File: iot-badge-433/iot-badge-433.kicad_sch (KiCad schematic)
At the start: 62 parts, among them J1 USB_C_Receptacle_USB2.0, J2 Wire ANT, Q1 BC847, Q2 BC847, Q3 BC847, SW1 SW_Push, SW2 SW_Push, SW3 SW_Push, SW4 SW_Push, SW5 SW_Push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

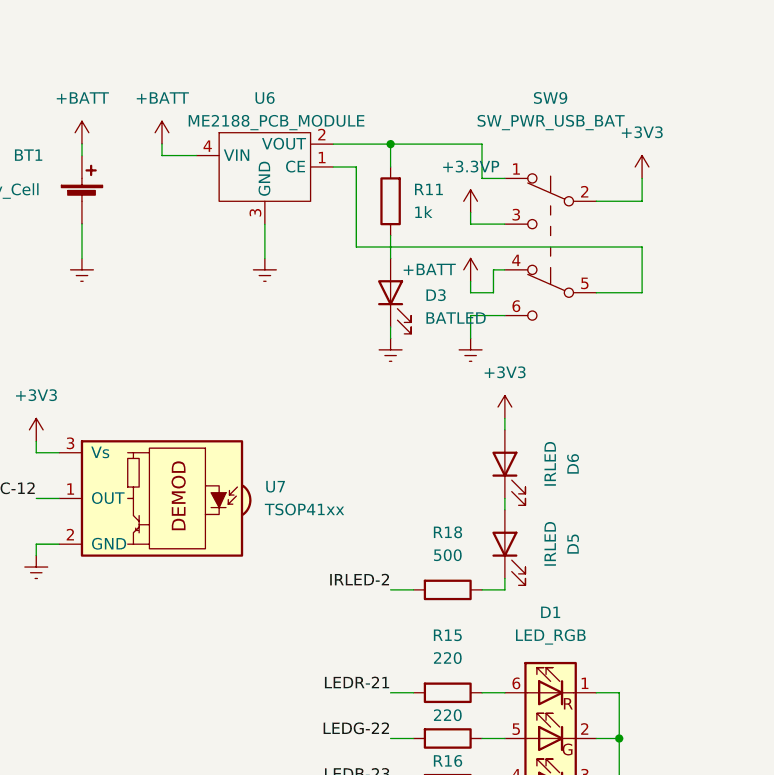
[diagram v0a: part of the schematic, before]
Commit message: changed ir leds polarity, PSU silk and bypass jumper
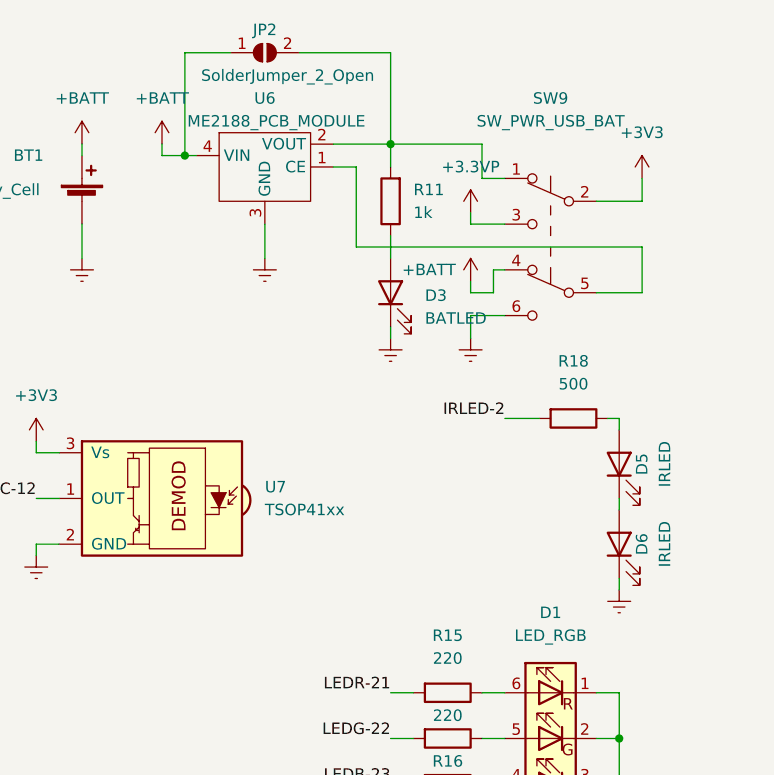
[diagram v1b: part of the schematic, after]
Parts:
- added JP2: SolderJumper_2_Open, Jumper:SolderJumper-2_P1.3mm_Open_RoundedPad1.0x1.5mm, symbol Jumper:SolderJumper_2_Open
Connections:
- net +3V3: no longer D6.2 (A)
- net +BATT: now also JP2.1 (A)
- net Earth: now also D6.1 (K)
- net at R11.2, SW9.1 (A), U6.2 (VOUT): now also JP2.2 (B)
- net at D5.1 (K): now also D6.2 (A); no longer R18.1
- net at D5.2 (A): now also R18.1; no longer D6.1 (K)
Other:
- moved on the sheet: D5, D6, R18

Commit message: added external i2c pins
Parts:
- added J3: Conn_01x04_Male, Connector_PinHeader_2.54mm:PinHeader_1x04_P2.54mm_Vertical, symbol Connector:Conn_01x04_Male
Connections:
- net +3V3: now also J3.2 (Pin_2)
- net Earth: now also J3.1 (Pin_1)
- net SCL: now reaches R6.2, U1.23 (IO15), U3.3 (SCL)
- net SCL: now also J3.3 (Pin_3)
- net SDA: now reaches R7.2, U1.26 (IO4), U3.4 (SDA)
- net SDA: now also J3.4 (Pin_4)
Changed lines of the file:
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@@
+    (stroke (width 0) (type default) (color 0 0 0 0))
+  )
+  (wire (pts (xy 139.7 30.48) (xy 146.05 30.48))
     (stroke (width 0) (type default) (color 0 0 0 0))
   )
@@
     (stroke (width 0) (type default) (color 0 0 0 0))
   )
+  (wire (pts (xy 144.78 33.02) (xy 146.05 33.02))
+    (stroke (width 0) (type default) (color 0 0 0 0))
+  )
   (wire (pts (xy 254 44.45) (xy 250.19 44.45))
     (stroke (width 0) (type default) (color 0 0 0 0))
@@
     (stroke (width 0) (type default) (color 0 0 0 0))
   )
+  (wire (pts (xy 139.7 36.83) (xy 139.7 30.48))
+    (stroke (width 0) (type default) (color 0 0 0 0))
+  )
   (wire (pts (xy 115.57 176.53) (xy 115.57 177.8))
     (stroke (width 0) (type default) (color 0 0 0 0))
@@
     (stroke (width 0) (type default) (color 0 0 0 0))
   )
+  (wire (pts (xy 135.89 36.83) (xy 139.7 36.83))
+    (stroke (width 0) (type default) (color 0 0 0 0))
+  )
   (wire (pts (xy 99.06 149.86) (xy 110.49 149.86))
     (stroke (width 0) (type default) (color 0 0 0 0))
@@
     (stroke (width 0) (type default) (color 0 0 0 0))
   )
+  (wire (pts (xy 135.89 27.94) (xy 146.05 27.94))
+    (stroke (width 0) (type default) (color 0 0 0 0))
+  )
   (wire (pts (xy 165.1 162.56) (xy 167.64 162.56))
     (stroke (width 0) (type default) (color 0 0 0 0))
@@
     (stroke (width 0) (type default) (color 0 0 0 0))
   )
+  (wire (pts (xy 135.89 35.56) (xy 135.89 36.83))
+    (stroke (width 0) (type default) (color 0 0 0 0))
+  )
   (wire (pts (xy 71.12 120.65) (xy 147.32 120.65))
+    (stroke (width 0) (type default) (color 0 0 0 0))
+  )
+  (wire (pts (xy 144.78 35.56) (xy 146.05 35.56))
     (stroke (width 0) (type default) (color 0 0 0 0))
   )
@@
     (effects (font (size 1.27 1.27)) (justify left bottom))
   )
+  (label "SCL" (at 118.11 60.96 180)
+    (effects (font (size 1.27 1.27)) (justify right bottom))
+  )
+  (label "SDA" (at 118.11 55.88 180)
+    (effects (font (size 1.27 1.27)) (justify right bottom))
+  )
   (label "LEDB-23" (at 241.3 96.52 180)
     (effects (font (size 1.27 1.27)) (justify right bottom))
@@
     (effects (font (size 1.27 1.27)) (justify left bottom))
   )
+  (label "SCL" (at 144.78 33.02 180)
+    (effects (font (size 1.27 1.27)) (justify right bottom))
+  )
   (label "SW4-17" (at 217.17 157.48 180)
     (effects (font (size 1.27 1.27)) (justify right bottom))
@@
   (label "SW3-16" (at 67.31 71.12 0)
     (effects (font (size 1.27 1.27)) (justify left bottom))
+  )
+  (label "SDA" (at 144.78 35.56 180)
+    (effects (font (size 1.27 1.27)) (justify right bottom))
   )
   (label "IRLED-2" (at 254 55.88 180)
@@
     (pin "1")
   )
+  (symbol (lib_id "power:Earth") (at 135.89 27.94 0) (unit 1)
+    (in_bom yes) (on_board yes) (fields_autoplaced)
+    (property "Reference" "#PWR0137" (id 0) (at 135.89 34.29 0)
+      (effects (font (size 1.27 1.27)) hide)
+    )
+    (property "Value" "Earth" (id 1) (at 135.89 31.75 0)
+      (effects (font (size 1.27 1.27)) hide)
+    )
+    (property "Footprint" "" (id 2) (at 135.89 27.94 0)
+      (effects (font (size 1.27 1.27)) hide)
+    )
+    (property "Datasheet" "~" (id 3) (at 135.89 27.94 0)
+      (effects (font (size 1.27 1.27)) hide)
+    )
+    (pin "1")
+  )
   (symbol (lib_id "Device:C") (at 237.49 127 0) (unit 1)
     (in_bom yes) (on_board yes)
@@
     (pin "1")
     (pin "2")
+  )
+  (symbol (lib_id "power:+3V3") (at 135.89 35.56 0) (unit 1)
+    (in_bom yes) (on_board yes)
+    (property "Reference" "#PWR0138" (id 0) (at 135.89 39.37 0)
+      (effects (font (size 1.27 1.27)) hide)
+    )
+    (property "Value" "+3V3" (id 1) (at 132.08 34.29 0))
+    (property "Footprint" "" (id 2) (at 135.89 35.56 0)
+      (effects (font (size 1.27 1.27)) hide)
+    )
+    (property "Datasheet" "" (id 3) (at 135.89 35.56 0)
+      (effects (font (size 1.27 1.27)) hide)
+    )
+    (pin "1")
   )
   (symbol (lib_id "power:+3V3") (at 257.81 110.49 0) (unit 1)
@@
     )
     (pin "1")
+  )
+  (symbol (lib_id "Connector:Conn_01x04_Male") (at 151.13 30.48 0) (mirror y) (unit 1)
+    (in_bom yes) (on_board yes) (fields_autoplaced)
+    (property "Reference" "J3" (id 0) (at 152.4 30.4799 0)
+      (effects (font (size 1.27 1.27)) (justify right))
+    )
+    (property "Value" "Conn_01x04_Male" (id 1) (at 152.4 33.0199 0)
+      (effects (font (size 1.27 1.27)) (justify right))
+    )
+    (property "Footprint" "Connector_PinHeader_2.54mm:PinHeader_1x04_P2.54mm_Vertical" (id 2) (at 151.13 30.48 0)
+      (effects (font (size 1.27 1.27)) hide)
+    )
+    (property "Datasheet" "~" (id 3) (at 151.13 30.48 0)
+      (effects (font (size 1.27 1.27)) hide)
+    )
+    (pin "1")
+    (pin "2")
+    (pin "3")
+    (pin "4")
   )
   (symbol (lib_id "Device:R") (at 29.21 40.64 0) (unit 1)
@@
       (reference "#PWR0136") (unit 1) (value "+3V3") (footprint "")
     )
+    (path "/4abb51ab-f7b7-4595-a1c4-f54294e1fb2f"
+      (reference "#PWR0137") (unit 1) (value "Earth") (footprint "")
+    )
+    (path "/54de0ed9-2c8d-4cc9-b91a-f024e43a8d70"
+      (reference "#PWR0138") (unit 1) (value "+3V3") (footprint "")
+    )
     (path "/17a036a7-3c7d-4750-8cd7-b5f99a19695c"
       (reference "AE1") (unit 1) (value "Antenna 433") (footprint "RF_PCB_Antenna:Micrel_Heli_2")
@@
       (reference "J2") (unit 1) (value "Wire ANT") (footprint "Connector_PinHeader_1.00mm:PinHeader_1x01_P1.00mm_Vertical")
     )
+    (path "/61aa9edf-d0b2-4bf3-b2ce-594476bcc882"
+      (reference "J3") (unit 1) (value "Conn_01x04_Male") (footprint "Connector_PinHeader_2.54mm:PinHeader_1x04_P2.54mm_Vertical")
+    )
     (path "/318e1c86-18c7-41e9-9cf9-b63eea81900c"

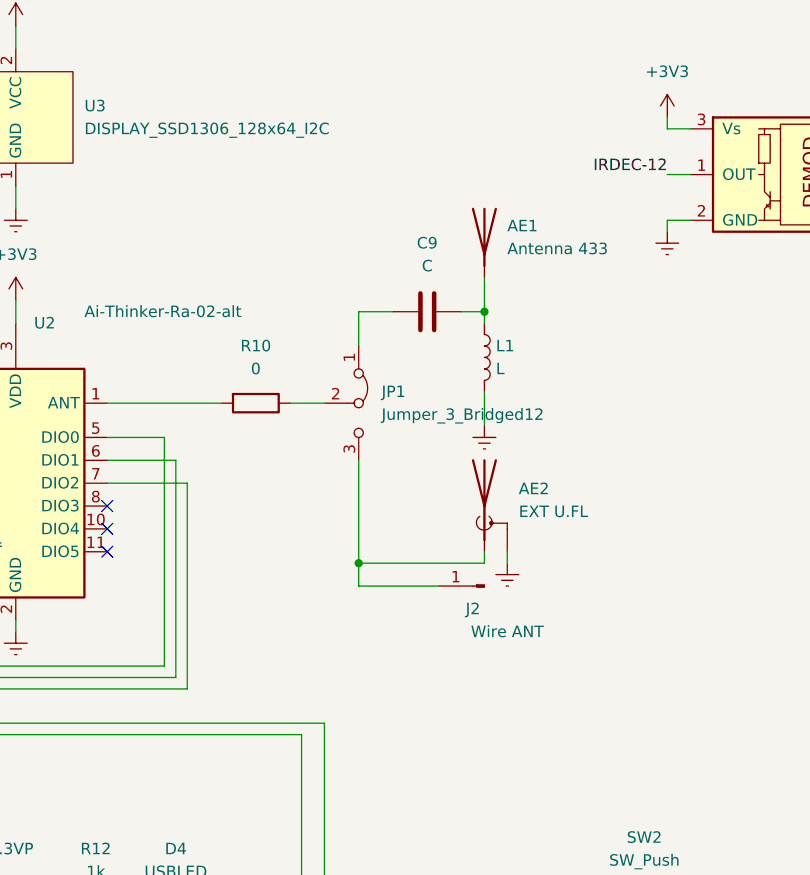
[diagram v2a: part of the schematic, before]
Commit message: added tuning cap an inductor to ant circuit
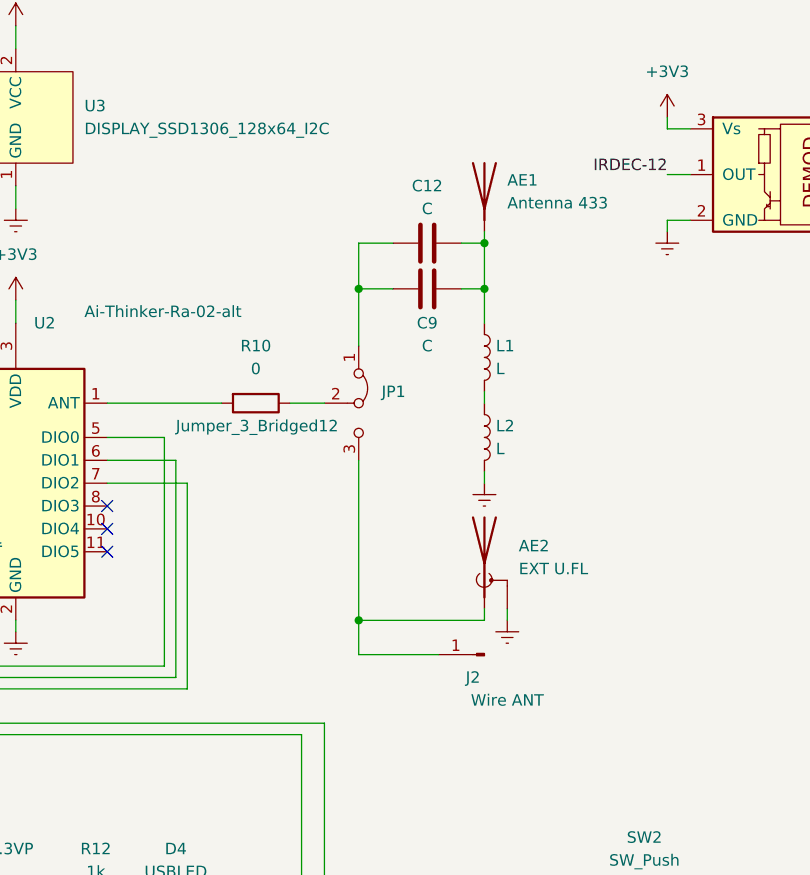
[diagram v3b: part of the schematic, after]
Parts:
- added C12: C, Capacitor_SMD:C_0805_2012Metric_Pad1.18x1.45mm_HandSolder, symbol Device:C
- added L2: L, Inductor_SMD:L_0805_2012Metric_Pad1.05x1.20mm_HandSolder, symbol Device:L
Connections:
- net Earth: now also L2.2; no longer L1.2
- net at AE1.1 (A), C9.1, L1.1: now also C12.1
- net at C9.2, JP1.1 (A): now also C12.2
- new net: L1.2, L2.1
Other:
- moved on the sheet: AE1, AE2, C9, J2

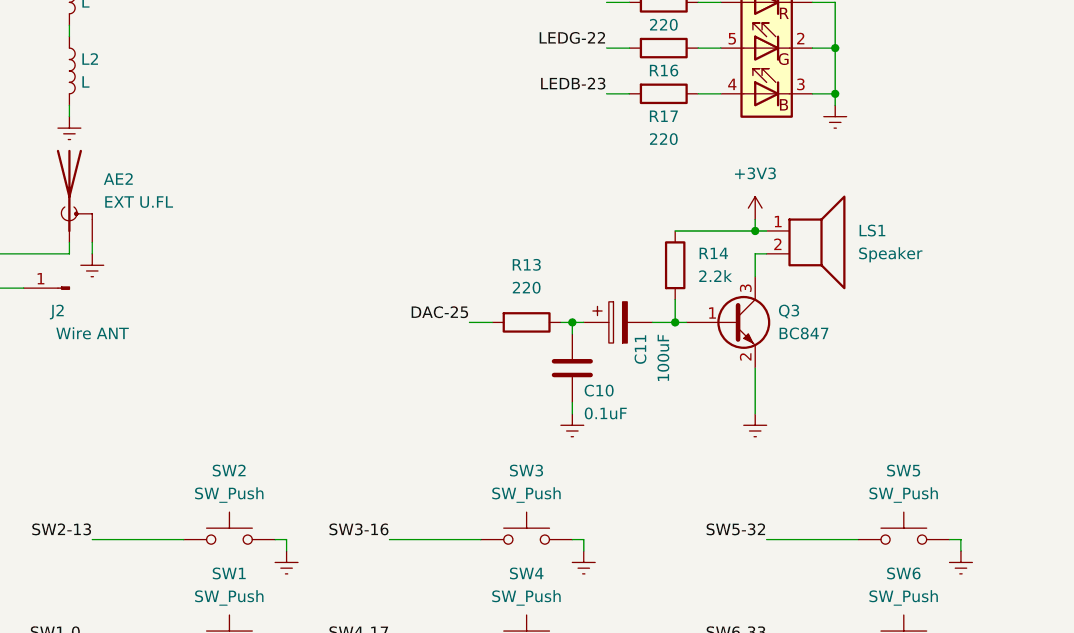
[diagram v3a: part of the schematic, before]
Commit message: added BTL amp to schematic
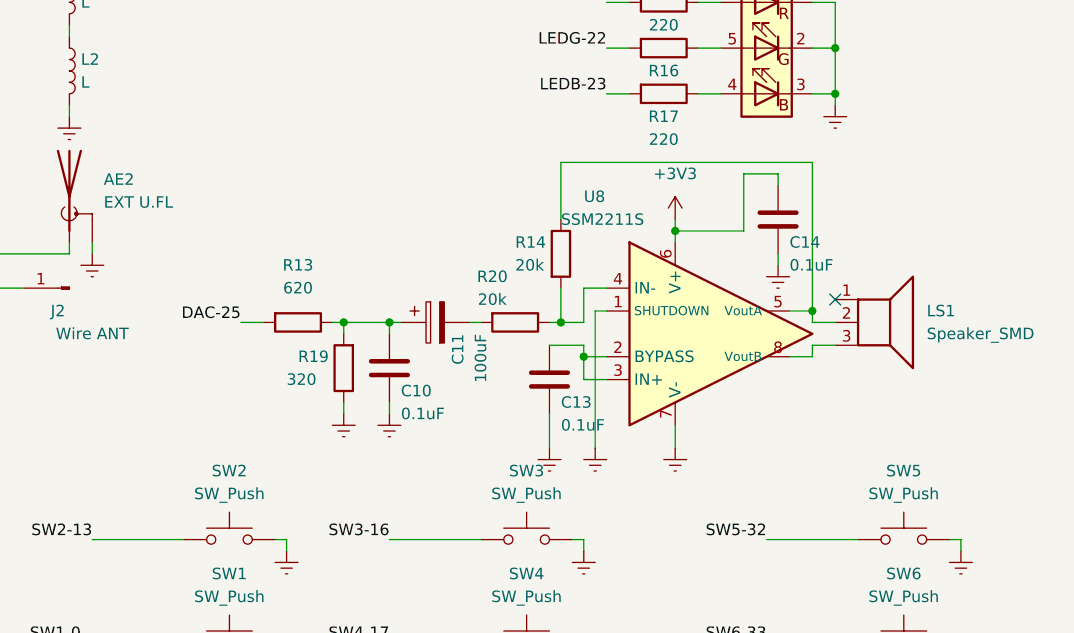
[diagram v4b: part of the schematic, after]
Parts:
- removed LS1: Speaker, Speaker_SMD:Speaker_SMD-10mmx5mm, symbol Device:Speaker
- removed Q3: BC847, Package_TO_SOT_SMD:SOT-23, symbol Transistor_BJT:BC847
- added C13, C14: 0.1uF, Capacitor_SMD:C_0805_2012Metric_Pad1.18x1.45mm_HandSolder, symbol Device:C
- added LS1: Speaker_SMD, Speaker_SMD:Speaker_SMD-5020, symbol Speaker_SMD:Speaker_SMD
- added R19: 320, Resistor_SMD:R_0805_2012Metric_Pad1.20x1.40mm_HandSolder, symbol Device:R
- added R20: 20k, Resistor_SMD:R_0805_2012Metric_Pad1.20x1.40mm_HandSolder, symbol Device:R
- added U8: SSM2211S, Package_SO:SOIC-8_3.9x4.9mm_P1.27mm, symbol Amplifier_Audio:SSM2211S
- R13: value 220 -> 620
- R14: value 2.2k -> 20k
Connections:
- net +3V3: now also C14.1, U8.6 (V+); no longer R14.1
- net Earth: now also C13.2, C14.2, R19.1, U8.1 (SHUTDOWN), U8.7 (V-)
- net at R14.2: now also R20.1, U8.4 (IN-); no longer C11.2
- net at C10.1, C11.1, R13.1: now also R19.2
- new net: LS1.2, R14.1, U8.5 (VoutA)
- new net: LS1.3, U8.8 (VoutB)
- new net: C13.1, U8.2 (BYPASS), U8.3 (IN+)
- new net: C11.2, R20.2
- no-connect marks 19 -> 20
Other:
- moved on the sheet: C10, C11, R13, R14

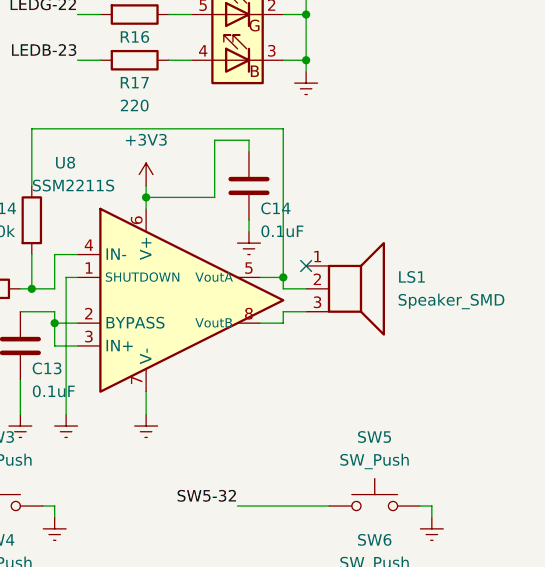
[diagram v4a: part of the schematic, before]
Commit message: audio amp elements routed
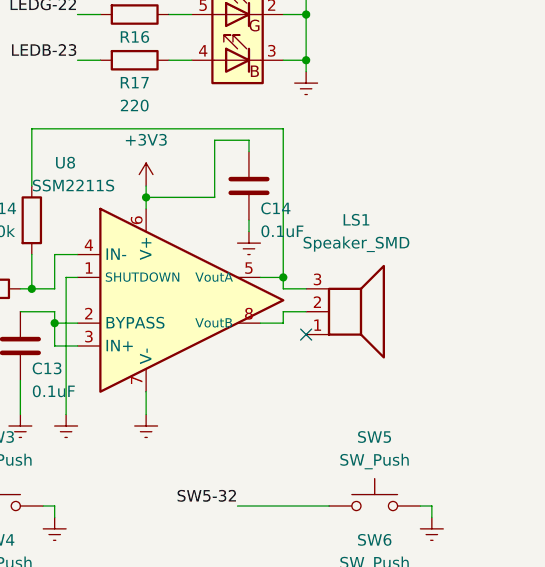
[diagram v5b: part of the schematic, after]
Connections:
- net at R14.1, U8.5 (VoutA): now also LS1.3; no longer LS1.2
- net at U8.8 (VoutB): now also LS1.2; no longer LS1.3
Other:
- moved on the sheet: LS1
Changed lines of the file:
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@@
   (no_connect (at 34.29 81.28))
   (no_connect (at 34.29 78.74))
-  (no_connect (at 266.7 119.38))
   (no_connect (at 34.29 88.9))
   (no_connect (at 138.43 166.37))
@@
   (no_connect (at 139.7 106.68))
   (no_connect (at 118.11 158.75))
+  (no_connect (at 266.7 127))
   (no_connect (at 34.29 50.8))
   (no_connect (at 20.32 187.96))
@@
     (stroke (width 0) (type default) (color 0 0 0 0))
   )
+  (wire (pts (xy 264.16 121.92) (xy 266.7 121.92))
+    (stroke (width 0) (type default) (color 0 0 0 0))
+  )
   (wire (pts (xy 156.21 182.88) (xy 157.48 182.88))
     (stroke (width 0) (type default) (color 0 0 0 0))
@@
     (stroke (width 0) (type default) (color 0 0 0 0))
   )
+  (wire (pts (xy 264.16 124.46) (xy 266.7 124.46))
+    (stroke (width 0) (type default) (color 0 0 0 0))
+  )
   (wire (pts (xy 80.01 76.2) (xy 80.01 101.6))
     (stroke (width 0) (type default) (color 0 0 0 0))
@@
     (stroke (width 0) (type default) (color 0 0 0 0))
   )
-  (wire (pts (xy 266.7 121.92) (xy 264.16 121.92))
-    (stroke (width 0) (type default) (color 0 0 0 0))
-  )
   (wire (pts (xy 64.77 53.34) (xy 85.09 53.34))
     (stroke (width 0) (type default) (color 0 0 0 0))
@@
   )
   (wire (pts (xy 138.43 176.53) (xy 143.51 176.53))
-    (stroke (width 0) (type default) (color 0 0 0 0))
-  )
-  (wire (pts (xy 264.16 124.46) (xy 266.7 124.46))
     (stroke (width 0) (type default) (color 0 0 0 0))
   )
@@
     (pin "2")
   )
-  (symbol (lib_id "Speaker_SMD:Speaker_SMD") (at 271.78 120.65 0) (unit 1)
-    (in_bom yes) (on_board yes) (fields_autoplaced)
-    (property "Reference" "LS1" (id 0) (at 276.86 120.6499 0)
-      (effects (font (size 1.27 1.27)) (justify left))
-    )
-    (property "Value" "Speaker_SMD" (id 1) (at 276.86 123.1899 0)
-      (effects (font (size 1.27 1.27)) (justify left))
-    )
-    (property "Footprint" "Speaker_SMD:Speaker_SMD-5020" (id 2) (at 271.78 125.73 0)
-      (effects (font (size 1.27 1.27)) hide)
-    )
-    (property "Datasheet" "~" (id 3) (at 271.526 121.92 0)
-      (effects (font (size 1.27 1.27)) hide)
-    )
+  (symbol (lib_id "Speaker_SMD:Speaker_SMD") (at 271.78 125.73 0) (mirror x) (unit 1)
+    (in_bom yes) (on_board yes) (fields_autoplaced)
+    (property "Reference" "LS1" (id 0) (at 272.288 114.3 0))
+    (property "Value" "Speaker_SMD" (id 1) (at 272.288 116.84 0))
+    (property "Footprint" "Speaker_SMD:Speaker_SMD-5020" (id 2) (at 271.78 120.65 0)
+      (effects (font (size 1.27 1.27)) hide)
+    )
+    (property "Datasheet" "~" (id 3) (at 271.526 124.46 0)
+      (effects (font (size 1.27 1.27)) hide)
+    )
